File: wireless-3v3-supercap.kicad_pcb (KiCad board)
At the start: 2 copper layers, 88 x 40 mm, 17 parts, among them J1 Conn_01x05_Pin

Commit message: Fix pin header name and size
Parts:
- J1: value Conn_01x05_Pin -> POWER-OUT
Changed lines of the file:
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@@
 			)
 		)
-		(property "Value" "Conn_01x05_Pin"
-			(at 0 12.54 90)
-			(layer "F.Fab")
+		(property "Value" "POWER-OUT"
+			(at 2.54 5.08 180)
+			(layer "F.SilkS")
 			(effects
 				(font

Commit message: Add xkcd comic
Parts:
- added XKCD: LOGO, LOGO, B.Cu at (43.8, 44.5)
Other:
- board text added: "xkcd.com/3106 ~{ }"

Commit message: Add incomplete charge circuit
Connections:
- C.U1 pad 17: unconnected-(C.U1-EP-Pad17) -> GND
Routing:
- net GND: vias 36 -> 45

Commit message: Add PCB OID and URL
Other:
- board text added: "https://pcb.nom.is/wireless-3v3-supercap"
- board text added: "urn:oid:1.3.6.1.4.1.39777.1.3.3.1.0"
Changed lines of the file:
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@@
+		)
+	)
+	(gr_text "https://pcb.nom.is/wireless-3v3-supercap"
+		(at 29.21 26.67 0)
+		(layer "B.SilkS")
+		(effects
+			(font
+				(size 1 1)
+				(thickness 0.2)
+				(bold yes)
+			)
+			(justify right top mirror)
+		)
+	)
+	(gr_text "urn:oid:1.3.6.1.4.1.39777.1.3.3.1.0"
+		(at 109.855 26.67 0)
+		(layer "B.SilkS")
+		(effects
+			(font
+				(size 1 1)
+				(thickness 0.2)
+				(bold yes)
+			)
+			(justify left top mirror)
 		)
 	)

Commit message: Add JLC order number text
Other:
- board text added: "JLCJLCJLCJLC"
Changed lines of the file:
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@@
+		)
+	)
+	(gr_text "JLCJLCJLCJLC"
+		(at 27.305 46.99 270)
+		(layer "B.SilkS")
+		(effects
+			(font
+				(size 1.5 1.5)
+				(thickness 0.3)
+				(bold yes)
+			)
+			(justify mirror)
 		)
 	)

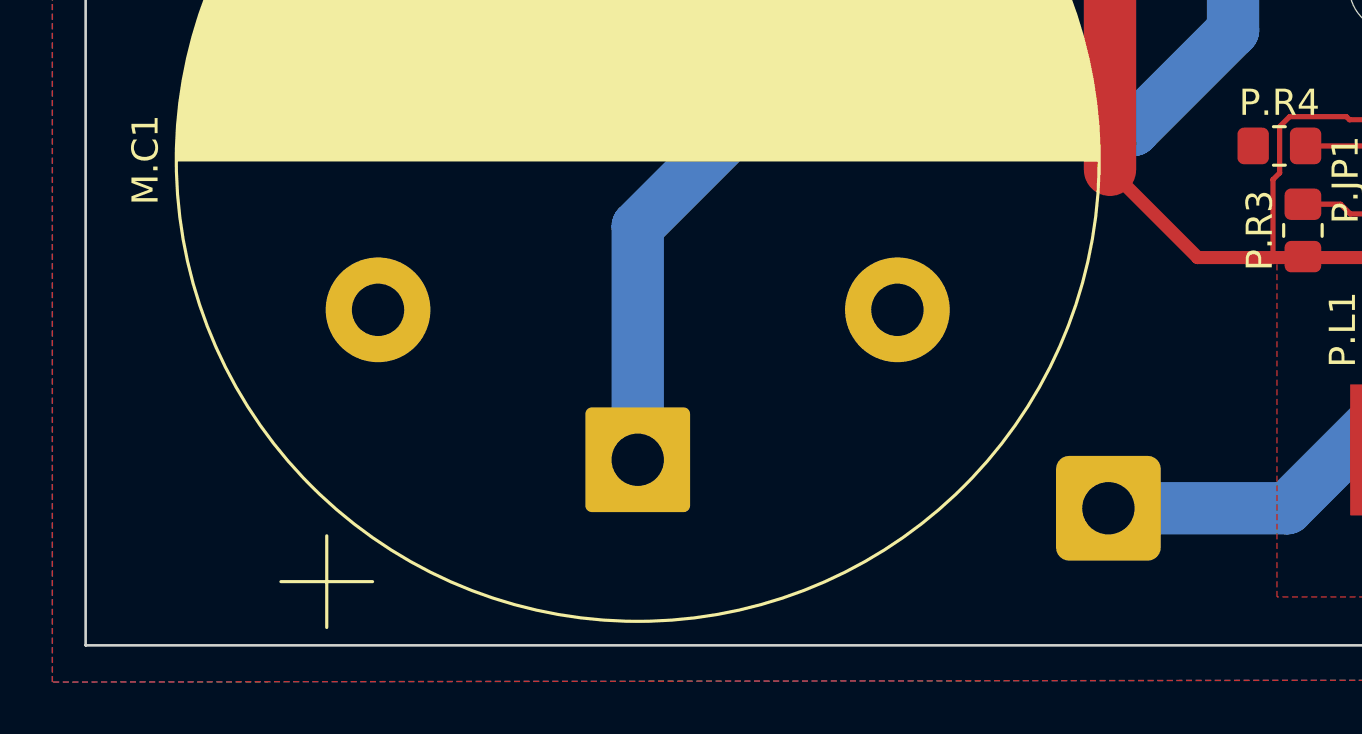
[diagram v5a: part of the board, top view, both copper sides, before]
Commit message: Add Area X crawler text quote underneath the topographical anomaly
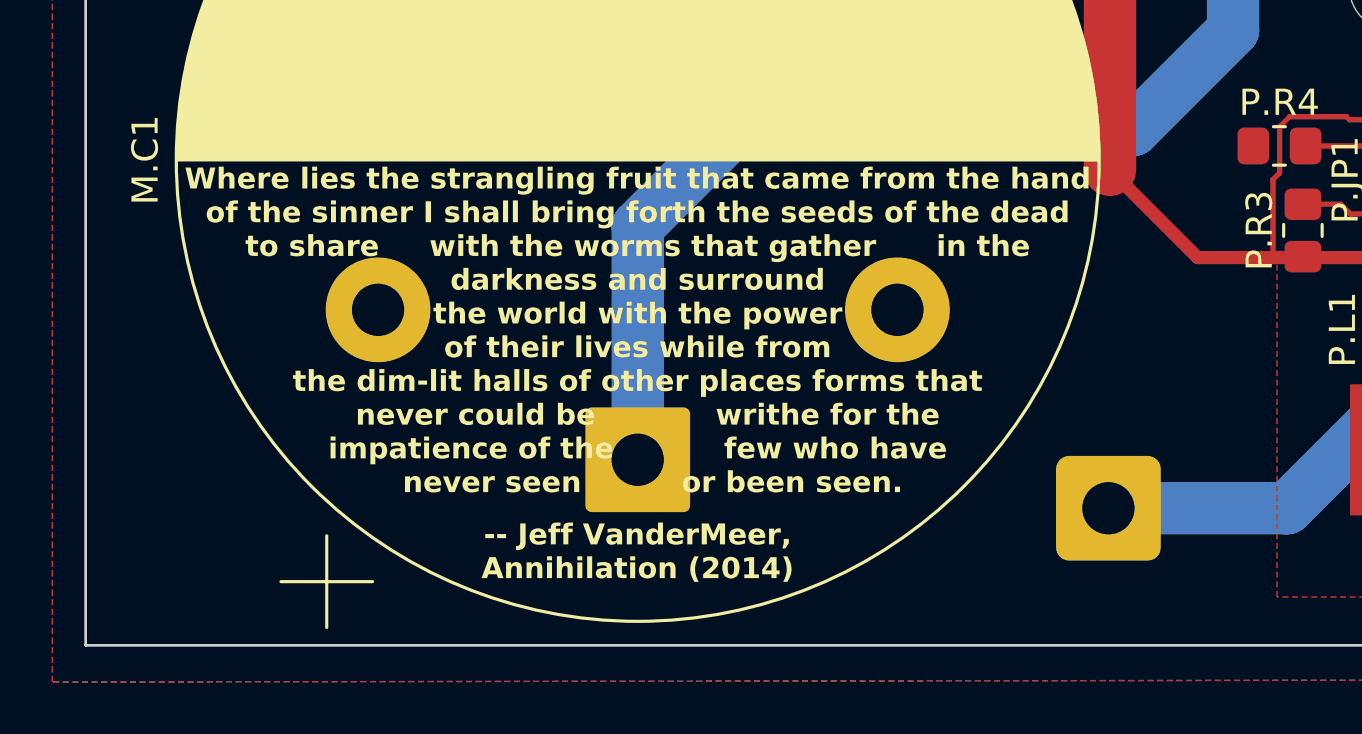
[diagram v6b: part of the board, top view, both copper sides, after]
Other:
- board text added: "-- Jeff VanderMeer, Annihilation (2014)"
- board text added: "Where lies the strangling fruit that came from the hand of the sinner I shall bring forth the seeds of the dead to share with the worms that gather in the darkness and surround the world with the power of their lives while from the dim-lit halls of other places forms that never could be writhe for the impatience of the few who have never seen or been seen."
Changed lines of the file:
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@@
+		)
+	)
+	(gr_text "Where lies the strangling fruit that came from the hand\nof the sinner I shall bring forth the seeds of the dead\nto share     with the worms that gather      in the  \ndarkness and surround\nthe world with the power\nof their lives while from\nthe dim-lit halls of other places forms that\n  never could be            writhe for the \nimpatience of the           few who have \n   never seen          or been seen."
+		(at 46.482 47.117 0)
+		(layer "F.SilkS")
+		(effects
+			(font
+				(size 0.8 0.8)
+				(thickness 0.16)
+				(bold yes)
+			)
+			(justify top)
 		)
 	)
@@
 			)
 			(justify right)
+		)
+	)
+	(gr_text "-- Jeff VanderMeer,\nAnnihilation (2014) "
+		(at 46.482 60.706 0)
+		(layer "F.SilkS")
+		(effects
+			(font
+				(size 0.8 0.8)
+				(thickness 0.16)
+				(bold yes)
+			)
+			(justify top)
 		)
 	)
@@
 			(font
 				(size 1 1)
-				(thickness 0.1)
+				(thickness 0.15)
 			)
 			(justify mirror)

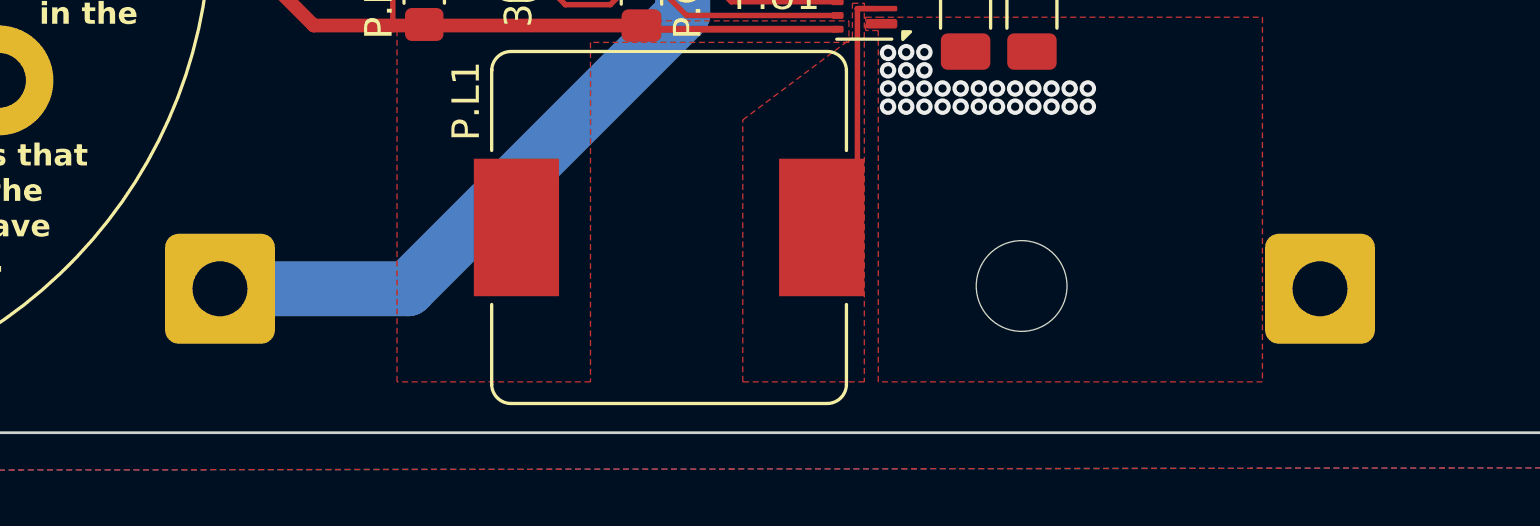
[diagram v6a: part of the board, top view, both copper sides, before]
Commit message: Update footprint of THS25R39J
This measures L=27.3mm M=44.8mm which is much smaller than the maximum
documented size. Retain the original sizes but move the pads closer
together to match the connection holes.
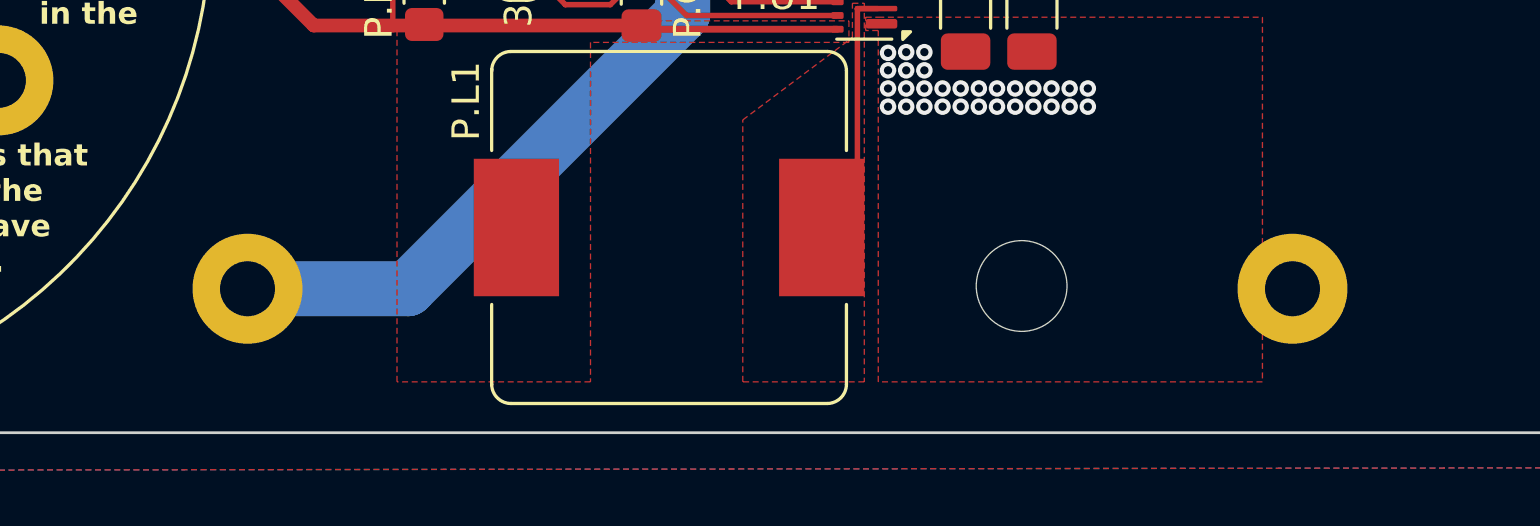
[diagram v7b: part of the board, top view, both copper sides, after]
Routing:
- net /DISCHARGE: track 45.2 -> 44.2 mm
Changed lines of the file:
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@@
+			(layer "Dwgs.User")
+			(pts
+				(xy 75.305 40.265) (xy 74.355 43.065)
+			)
+			(height -14.2)
+			(orientation 1)
+			(format
+				(prefix "R ")
+				(suffix "")
+				(units 2)
+				(units_format 1)
+				(precision 4)
+				(suppress_zeroes yes)
+			)
+			(style
+				(thickness 0.1)
+				(arrow_length 1.27)
+				(text_position_mode 0)
+				(arrow_direction outward)
+				(extension_height 0.58642)
+				(extension_offset 0.5)
+				(keep_text_aligned yes)
+			)
+			(gr_text "R 2.8 mm"
+				(at 60.005 41.665 90)
+				(layer "Dwgs.User")
+				(effects
+					(font
+						(size 1 1)
+						(thickness 0.1)
+					)
+				)
+			)
+		)
+		(dimension
+			(type orthogonal)
+			(layer "Dwgs.User")
+			(pts
+				(xy 110.355 50.165) (xy 58.555 50.165)
+			)
+			(height 28.3)
+			(orientation 0)
+			(format
+				(prefix "M ")
+				(suffix "")
+				(units 2)
+				(units_format 1)
+				(precision 4)
+				(suppress_zeroes yes)
+			)
+			(style
+				(thickness 0.1)
+				(arrow_length 1.27)
+				(text_position_mode 0)
+				(arrow_direction outward)
+				(extension_height 0.58642)
+				(extension_offset 0.5)
+				(keep_text_aligned yes)
+			)
+			(gr_text "M 51.8 mm"
+				(at 84.455 77.315 0)
+				(layer "Dwgs.User")
+				(effects
+					(font
+						(size 1 1)
+						(thickness 0.15)
+					)
+				)
+			)
+		)
+		(dimension
+			(type orthogonal)
+			(layer "Dwgs.User")
+			(pts
+				(xy 75.305 40.165) (xy 93.605 60.165)
+			)
+			(height 29.556)
+			(orientation 0)
+			(format
+				(prefix "H ")
+				(suffix "")
+				(units 2)
+				(units_format 1)
+				(precision 4)
+				(suppress_zeroes yes)
+			)
+			(style
+				(thickness 0.1)
+				(arrow_length 1.27)
+				(text_position_mode 0)
+				(arrow_direction outward)
+				(extension_height 0.58642)
+				(extension_offset 0.5)
+				(keep_text_aligned yes)
+			)
+			(gr_text "H 18.3 mm"
+				(at 84.455 68.621 0)
+				(layer "Dwgs.User")
+				(effects
+					(font
+						(size 1 1)
+						(thickness 0.1)
+					)
+				)
+			)
+		)
+		(dimension
+			(type orthogonal)
+			(layer "Dwgs.User")
+			(pts
+				(xy 65.455 60.165) (xy 103.455 60.165)
+			)
+			(height 23.5)
+			(orientation 0)
+			(format
+				(prefix "")
+				(suffix "")
+				(units 2)
+				(units_format 1)
+				(precision 4)
+				(suppress_zeroes yes)
+			)
+			(style
+				(thickness 0.1)
+				(arrow_length 1.27)
+				(text_position_mode 0)
+				(arrow_direction outward)
+				(extension_height 0.58642)
+				(extension_offset 0.5)
+				(keep_text_aligned yes)
+			)
+			(gr_text "38 mm"
+				(at 84.455 82.515 0)
+				(layer "Dwgs.User")
+				(effects
+					(font
+						(size 1 1)
+						(thickness 0.15)
+					)
+				)
+			)
+		)
+		(dimension
+			(type orthogonal)
+			(layer "Dwgs.User")
+			(pts
+				(xy 93.605 60.065) (xy 75.295 40.265)
+			)
+			(height -51.65)
+			(orientation 1)
+			(format
+				(prefix "J ")
+				(suffix "")
+				(units 2)
+				(units_format 1)
+				(precision 4)
+				(suppress_zeroes yes)
+			)
+			(style
+				(thickness 0.1)
+				(arrow_length 1.27)
+				(text_position_mode 0)
+				(arrow_direction outward)
+				(extension_height 0.58642)
+				(extension_offset 0.5)
+				(keep_text_aligned yes)
+			)
+			(gr_text "J 19.8 mm"
+				(at 40.855 50.165 90)
+				(layer "Dwgs.User")
+				(effects
+					(font
+						(size 1 1)
+						(thickness 0.1)
+					)
+				)
+			)
+		)
+		(dimension
+			(type orthogonal)
+			(layer "Dwgs.User")
+			(pts
+				(xy 93.655 57.265) (xy 93.605 60.065)
+			)
+			(height 6.7)
+			(orientation 1)
+			(format
+				(prefix "R ")
+				(suffix "")
+				(units 2)
+				(units_format 1)
+				(precision 4)
+				(suppress_zeroes yes)
+			)
+			(style
+				(thickness 0.1)
+				(arrow_length 1.27)
+				(text_position_mode 0)
+				(arrow_direction outward)
+				(extension_height 0.58642)
+				(extension_offset 0.5)
+				(keep_text_aligned yes)
+			)
+			(gr_text "R 2.8 mm"
+				(at 99.205 58.665 90)
+				(layer "Dwgs.User")
+				(effects
+					(font
+						(size 1 1)
+						(thickness 0.15)
+					)
+				)
+			)
+		)
+		(dimension
+			(type orthogonal)
 			(layer "Dwgs.User")
 			(pts
@@
 			(layer "Dwgs.User")
 			(pts
-				(xy 110.355 50.165) (xy 58.555 50.165)
-			)
-			(height 28.3)
-			(orientation 0)
-			(format
-				(prefix "M ")
-				(suffix "")
-				(units 2)
-				(units_format 1)
-				(precision 4)
-				(suppress_zeroes yes)
-			)
-			(style
-				(thickness 0.1)
-				(arrow_length 1.27)
-				(text_position_mode 0)
-				(arrow_direction outward)
-				(extension_height 0.58642)
-				(extension_offset 0.5)
-				(keep_text_aligned yes)
-			)
-			(gr_text "M 51.8 mm"
-				(at 84.455 77.315 0)
-				(layer "Dwgs.User")
-				(effects
-					(font
-						(size 1 1)
-						(thickness 0.15)
-					)
-				)
-			)
-		)
-		(dimension
-			(type orthogonal)
-			(layer "Dwgs.User")
-			(pts
 				(xy 98.955 50.165) (xy 69.955 51.665)
 			)
@@
 			)
 		)
-		(dimension
-			(type orthogonal)
-			(layer "Dwgs.User")
-			(pts
-				(xy 93.655 57.265) (xy 93.605 60.065)
-			)
-			(height 6.7)
-			(orientation 1)
-			(format
-				(prefix "R ")
-				(suffix "")
-				(units 2)
-				(units_format 1)
-				(precision 4)
-				(suppress_zeroes yes)
-			)
-			(style
-				(thickness 0.1)
-				(arrow_length 1.27)
-				(text_position_mode 0)
-				(arrow_direction outward)
-				(extension_height 0.58642)
-				(extension_offset 0.5)
-				(keep_text_aligned yes)
-			)
-			(gr_text "R 2.8 mm"
-				(at 99.205 58.665 90)
-				(layer "Dwgs.User")
-				(effects
-					(font
-						(size 1 1)
-						(thickness 0.15)
-					)
-				)
-			)
-		)
-		(dimension
-			(type orthogonal)
-			(layer "Dwgs.User")
-			(pts
-				(xy 75.305 40.165) (xy 93.605 60.165)
-			)
-			(height 29.556)
-			(orientation 0)
-			(format
-				(prefix "H ")
-				(suffix "")
-				(units 2)
-				(units_format 1)
-				(precision 4)
-				(suppress_zeroes yes)
-			)
-			(style
-				(thickness 0.1)
-				(arrow_length 1.27)
-				(text_position_mode 0)
-				(arrow_direction outward)
-				(extension_height 0.58642)
-				(extension_offset 0.5)
-				(keep_text_aligned yes)
-			)
-			(gr_text "H 18.3 mm"
-				(at 84.455 68.621 0)
-				(layer "Dwgs.User")
-				(effects
-					(font
-						(size 1 1)
-						(thickness 0.1)
-					)
-				)
-			)
-		)
-		(dimension
-			(type orthogonal)
-			(layer "Dwgs.User")
-			(pts
-				(xy 93.605 60.065) (xy 75.295 40.265)
-			)
-			(height -51.65)
-			(orientation 1)
-			(format
-				(prefix "J ")
-				(suffix "")
-				(units 2)
-				(units_format 1)
-				(precision 4)
-				(suppress_zeroes yes)
-			)
-			(style
-				(thickness 0.1)
-				(arrow_length 1.27)
-				(text_position_mode 0)
-				(arrow_direction outward)
-				(extension_height 0.58642)
-				(extension_offset 0.5)
-				(keep_text_aligned yes)
-			)
-			(gr_text "J 19.8 mm"
-				(at 40.855 50.165 90)
-				(layer "Dwgs.User")
-				(effects
-					(font
-						(size 1 1)
-						(thickness 0.1)
-					)
-				)
-			)
-		)
-		(dimension
-			(type orthogonal)
-			(layer "Dwgs.User")
-			(pts
-				(xy 75.305 40.265) (xy 74.355 43.065)
-			)
-			(height -14.2)
-			(orientation 1)
-			(format
-				(prefix "R ")
-				(suffix "")
-				(units 2)
-				(units_format 1)
-				(precision 4)
-				(suppress_zeroes yes)
-			)
-			(style
-				(thickness 0.1)
-				(arrow_length 1.27)
-				(text_position_mode 0)
-				(arrow_direction outward)
-				(extension_height 0.58642)
-				(extension_offset 0.5)
-				(keep_text_aligned yes)
-			)
-			(gr_text "R 2.8 mm"
-				(at 60.005 41.665 90)
-				(layer "Dwgs.User")
-				(effects
-					(font
-						(size 1 1)
-						(thickness 0.1)
-					)
-				)
-			)
-		)
 		(pad "" np_thru_hole circle
 			(at -9.15 -9.9 180)
@@
 			(zone_connect 0)
 		)
-		(pad "1" thru_hole roundrect
-			(at 20 -10 180)
+		(pad "1" thru_hole circle
+			(at 19 -10 180)
 			(size 4 4)
 			(drill 2)
 			(layers "*.Cu" "*.Mask")
 			(remove_unused_layers no)
-			(roundrect_rratio 0.125)
 			(net 7 "/DISCHARGE")
 			(pintype "passive")
 			(clearance 2)
 		)
-		(pad "2" thru_hole roundrect
-			(at -20 -10 180)
+		(pad "2" thru_hole circle
+			(at -19 -10 180)
 			(size 4 4)
 			(drill 2)
 			(layers "*.Cu" "*.Mask")
 			(remove_unused_layers no)
-			(roundrect_rratio 0.125)
 			(net 1 "GND")
 			(pintype "passive")
@@
 	)
 	(segment
+		(start 71.28 60.165)
+		(end 65.455 60.165)
+		(width 2)
+		(layer "B.Cu")
+		(net 7)
+	)
+	(segment
 		(start 81.28 50.165)
 		(end 81.28 34.925)
 		(width 2)
 		(layer "B.Cu")
-		(net 7)
-	)
-	(segment
-		(start 64.455 60.165)
-		(end 71.28 60.165)
-		(width 2)
-		(layer "B.Cu")
